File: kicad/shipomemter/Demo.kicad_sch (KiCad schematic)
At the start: 7 parts, among them J701 Conn_01x06_Pin, J702 Conn_01x06_Pin, J703 Conn_01x06_Pin, J704 Conn_01x06_Pin

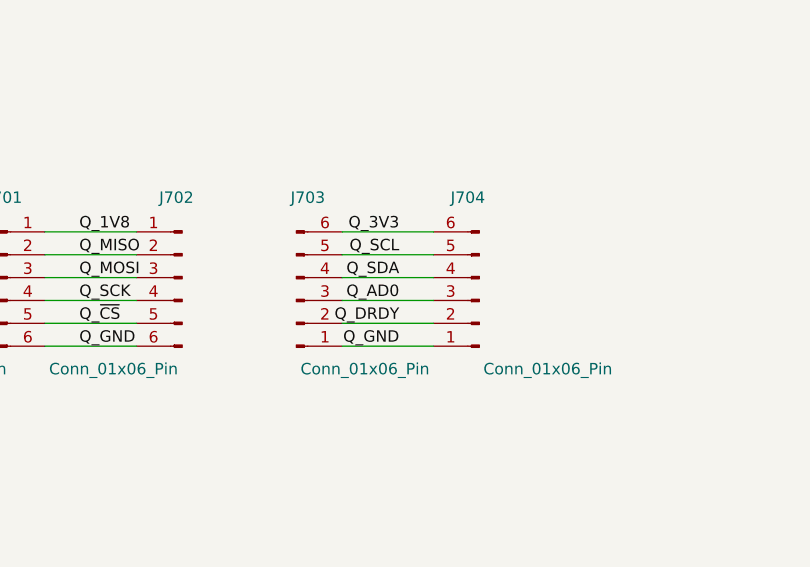
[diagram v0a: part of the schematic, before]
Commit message: Updated numbers on hand and numbers in cart
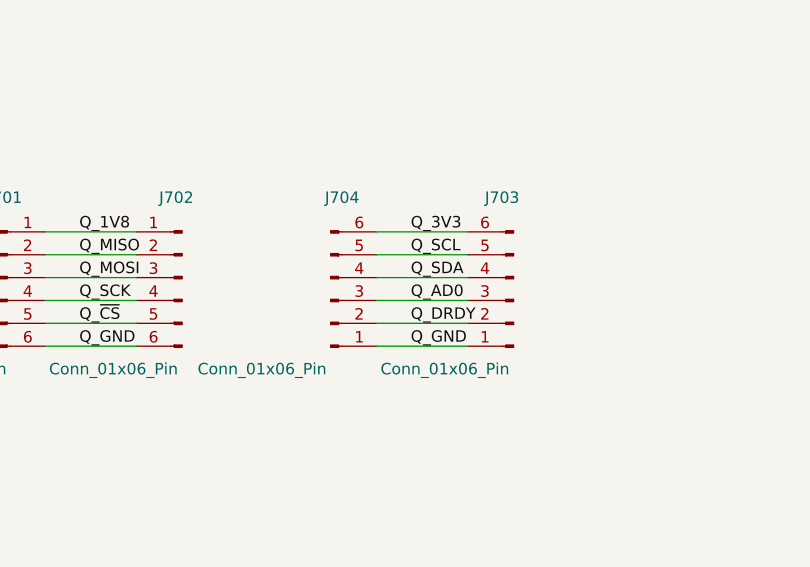
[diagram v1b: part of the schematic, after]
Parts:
- J701, J703: footprint Connector_PinHeader_2.54mm:PinHeader_1x06_P2.54mm_Vertical -> Connector_PinSocket_2.54mm:PinSocket_1x06_P2.54mm_Vertical; Mouser (none) -> 538-90147-1106; Number in cart (none) -> 2; Number on hand (none) -> 0
- J702, J704: Mouser (none) -> 855-M20-9990646; Number in cart (none) -> 2; Number on hand (none) -> 0
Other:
- moved on the sheet: J703, J704
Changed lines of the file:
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@@
   (junction (at 125.73 33.02) (diameter 0) (color 0 0 0 0)
   )
-  (wire (pts (xy 114.3 77.47) (xy 104.14 77.47))
+  (wire (pts (xy 107.95 77.47) (xy 118.11 77.47))
     (stroke (width 0) (type default))
   )
@@
     (stroke (width 0) (type default))
   )
-  (wire (pts (xy 114.3 80.01) (xy 104.14 80.01))
+  (wire (pts (xy 107.95 80.01) (xy 118.11 80.01))
     (stroke (width 0) (type default))
   )
@@
     (stroke (width 0) (type default))
   )
-  (wire (pts (xy 114.3 69.85) (xy 104.14 69.85))
-    (stroke (width 0) (type default))
-  )
-  (wire (pts (xy 114.3 74.93) (xy 104.14 74.93))
-    (stroke (width 0) (type default))
-  )
-  (wire (pts (xy 114.3 82.55) (xy 104.14 82.55))
+  (wire (pts (xy 107.95 69.85) (xy 118.11 69.85))
+    (stroke (width 0) (type default))
+  )
+  (wire (pts (xy 107.95 74.93) (xy 118.11 74.93))
+    (stroke (width 0) (type default))
+  )
+  (wire (pts (xy 107.95 82.55) (xy 118.11 82.55))
     (stroke (width 0) (type default))
   )
@@
     (stroke (width 0) (type default))
   )
-  (wire (pts (xy 114.3 72.39) (xy 104.14 72.39))
+  (wire (pts (xy 107.95 72.39) (xy 118.11 72.39))
     (stroke (width 0) (type default))
   )
@@
     (effects (font (size 1.27 1.27)) (justify left bottom))
   )
-  (label "Q_SCL" (at 110.49 72.39 180) (fields_autoplaced)
-    (effects (font (size 1.27 1.27)) (justify right bottom))
+  (label "Q_SCL" (at 111.76 72.39 0) (fields_autoplaced)
+    (effects (font (size 1.27 1.27)) (justify left bottom))
   )
   (label "Q_1V8" (at 74.93 69.85 0) (fields_autoplaced)
     (effects (font (size 1.27 1.27)) (justify left bottom))
   )
-  (label "Q_DRDY" (at 110.49 80.01 180) (fields_autoplaced)
-    (effects (font (size 1.27 1.27)) (justify right bottom))
-  )
-  (label "Q_3V3" (at 110.49 69.85 180) (fields_autoplaced)
-    (effects (font (size 1.27 1.27)) (justify right bottom))
+  (label "Q_DRDY" (at 111.76 80.01 0) (fields_autoplaced)
+    (effects (font (size 1.27 1.27)) (justify left bottom))
+  )
+  (label "Q_3V3" (at 111.76 69.85 0) (fields_autoplaced)
+    (effects (font (size 1.27 1.27)) (justify left bottom))
   )
   (label "Q_GND" (at 135.89 38.1 180) (fields_autoplaced)
@@
     (effects (font (size 1.27 1.27)) (justify left bottom))
   )
-  (label "Q_GND" (at 110.49 82.55 180) (fields_autoplaced)
-    (effects (font (size 1.27 1.27)) (justify right bottom))
-  )
-  (label "Q_SDA" (at 110.49 74.93 180) (fields_autoplaced)
-    (effects (font (size 1.27 1.27)) (justify right bottom))
+  (label "Q_GND" (at 111.76 82.55 0) (fields_autoplaced)
+    (effects (font (size 1.27 1.27)) (justify left bottom))
+  )
+  (label "Q_SDA" (at 111.76 74.93 0) (fields_autoplaced)
+    (effects (font (size 1.27 1.27)) (justify left bottom))
   )
   (label "Q_MISO" (at 74.93 72.39 0) (fields_autoplaced)
@@
     (effects (font (size 1.27 1.27)) (justify right bottom))
   )
-  (label "Q_AD0" (at 110.49 77.47 180) (fields_autoplaced)
-    (effects (font (size 1.27 1.27)) (justify right bottom))
+  (label "Q_AD0" (at 111.76 77.47 0) (fields_autoplaced)
+    (effects (font (size 1.27 1.27)) (justify left bottom))
   )
   (symbol (lib_id "KwanSystems:DesignedWithKicad") (at 212.09 173.99 0) (unit 1)
@@
     )
   )
-  (symbol (lib_id "Connector:Conn_01x06_Pin") (at 119.38 77.47 180) (unit 1)
-    (in_bom yes) (on_board yes) (dnp no)
-    (property "Reference" "J704" (at 118.11 66.04 0)
-      (effects (font (size 1.27 1.27)))
-    )
-    (property "Value" "Conn_01x06_Pin" (at 127 85.09 0)
-      (effects (font (size 1.27 1.27)))
-    )
-    (property "Footprint" "Connector_PinHeader_2.54mm:PinHeader_1x06_P2.54mm_Vertical" (at 119.38 77.47 0)
-      (effects (font (size 1.27 1.27)) hide)
-    )
-    (property "Datasheet" "~" (at 119.38 77.47 0)
+  (symbol (lib_id "Connector:Conn_01x06_Pin") (at 102.87 77.47 0) (mirror x) (unit 1)
+    (in_bom yes) (on_board yes) (dnp no)
+    (property "Reference" "J704" (at 104.14 66.04 0)
+      (effects (font (size 1.27 1.27)))
+    )
+    (property "Value" "Conn_01x06_Pin" (at 95.25 85.09 0)
+      (effects (font (size 1.27 1.27)))
+    )
+    (property "Footprint" "Connector_PinHeader_2.54mm:PinHeader_1x06_P2.54mm_Vertical" (at 102.87 77.47 0)
+      (effects (font (size 1.27 1.27)) hide)
+    )
+    (property "Datasheet" "~" (at 102.87 77.47 0)
+      (effects (font (size 1.27 1.27)) hide)
+    )
+    (property "Mouser" "855-M20-9990646" (at 102.87 77.47 0)
+      (effects (font (size 1.27 1.27)) hide)
+    )
+    (property "Number in cart" "2" (at 102.87 77.47 0)
+      (effects (font (size 1.27 1.27)) hide)
+    )
+    (property "Number on hand" "0" (at 102.87 77.47 0)
       (effects (font (size 1.27 1.27)) hide)
     )
@@
     )
   )
-  (symbol (lib_id "Connector:Conn_01x06_Pin") (at 99.06 77.47 0) (mirror x) (unit 1)
-    (in_bom yes) (on_board yes) (dnp no)
-    (property "Reference" "J703" (at 100.33 66.04 0)
-      (effects (font (size 1.27 1.27)))
-    )
-    (property "Value" "Conn_01x06_Pin" (at 106.68 85.09 0)
-      (effects (font (size 1.27 1.27)))
-    )
-    (property "Footprint" "Connector_PinHeader_2.54mm:PinHeader_1x06_P2.54mm_Vertical" (at 99.06 77.47 0)
-      (effects (font (size 1.27 1.27)) hide)
-    )
-    (property "Datasheet" "~" (at 99.06 77.47 0)
+  (symbol (lib_id "Connector:Conn_01x06_Pin") (at 123.19 77.47 180) (unit 1)
+    (in_bom yes) (on_board yes) (dnp no)
+    (property "Reference" "J703" (at 121.92 66.04 0)
+      (effects (font (size 1.27 1.27)))
+    )
+    (property "Value" "Conn_01x06_Pin" (at 115.57 85.09 0)
+      (effects (font (size 1.27 1.27)))
+    )
+    (property "Footprint" "Connector_PinSocket_2.54mm:PinSocket_1x06_P2.54mm_Vertical" (at 123.19 77.47 0)
+      (effects (font (size 1.27 1.27)) hide)
+    )
+    (property "Datasheet" "~" (at 123.19 77.47 0)
+      (effects (font (size 1.27 1.27)) hide)
+    )
+    (property "Mouser" "538-90147-1106" (at 123.19 77.47 0)
+      (effects (font (size 1.27 1.27)) hide)
+    )
+    (property "Number in cart" "2" (at 123.19 77.47 0)
+      (effects (font (size 1.27 1.27)) hide)
+    )
+    (property "Number on hand" "0" (at 123.19 77.47 0)
       (effects (font (size 1.27 1.27)) hide)
     )
@@
       (effects (font (size 1.27 1.27)) hide)
     )
+    (property "Mouser" "855-M20-9990646" (at 86.36 74.93 0)
+      (effects (font (size 1.27 1.27)) hide)
+    )
+    (property "Number in cart" "2" (at 86.36 74.93 0)
+      (effects (font (size 1.27 1.27)) hide)
+    )
+    (property "Number on hand" "0" (at 86.36 74.93 0)
+      (effects (font (size 1.27 1.27)) hide)
+    )
     (pin "1")
     (pin "2")
@@
       (effects (font (size 1.27 1.27)))
     )
-    (property "Footprint" "Connector_PinHeader_2.54mm:PinHeader_1x06_P2.54mm_Vertical" (at 66.04 74.93 0)
+    (property "Footprint" "Connector_PinSocket_2.54mm:PinSocket_1x06_P2.54mm_Vertical" (at 66.04 74.93 0)
       (effects (font (size 1.27 1.27)) hide)
     )
@@
       (effects (font (size 1.27 1.27)) hide)
     )
+    (property "Mouser" "538-90147-1106" (at 66.04 74.93 0)
+      (effects (font (size 1.27 1.27)) hide)
+    )
+    (property "Number in cart" "2" (at 66.04 74.93 0)
+      (effects (font (size 1.27 1.27)) hide)
+    )
+    (property "Number on hand" "0" (at 66.04 74.93 0)
+      (effects (font (size 1.27 1.27)) hide)
+    )

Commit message: Updated number on hand, and added more Digikey/Mouser/Mfg numbers
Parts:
- J701, J703: Digikey (none) -> WM4223-ND; Number in cart 2 -> (none); Number on hand 0 -> 2; Part Number (none) -> 90147-1106
- J702, J704: Digikey (none) -> 952-2270-ND; Number in cart 2 -> (none); Number on hand 0 -> 2; Part Number (none) -> M20-9990646
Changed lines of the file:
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@@
       (effects (font (size 1.27 1.27)) hide)
     )
-    (property "Number in cart" "2" (at 102.87 77.47 0)
+    (property "Number in cart" "" (at 102.87 77.47 0)
       (effects (font (size 1.27 1.27)) hide)
     )
-    (property "Number on hand" "0" (at 102.87 77.47 0)
+    (property "Number on hand" "2" (at 102.87 77.47 0)
+      (effects (font (size 1.27 1.27)) hide)
+    )
+    (property "Digikey" "952-2270-ND" (at 102.87 77.47 0)
+      (effects (font (size 1.27 1.27)) hide)
+    )
+    (property "Part Number" "M20-9990646" (at 102.87 77.47 0)
       (effects (font (size 1.27 1.27)) hide)
     )
@@
       (effects (font (size 1.27 1.27)) hide)
     )
-    (property "Number in cart" "2" (at 123.19 77.47 0)
+    (property "Number in cart" "" (at 123.19 77.47 0)
       (effects (font (size 1.27 1.27)) hide)
     )
-    (property "Number on hand" "0" (at 123.19 77.47 0)
+    (property "Number on hand" "2" (at 123.19 77.47 0)
+      (effects (font (size 1.27 1.27)) hide)
+    )
+    (property "Part Number" "90147-1106" (at 123.19 77.47 0)
+      (effects (font (size 1.27 1.27)) hide)
+    )
+    (property "Digikey" "WM4223-ND" (at 123.19 77.47 0)
       (effects (font (size 1.27 1.27)) hide)
     )
@@
       (effects (font (size 1.27 1.27)) hide)
     )
-    (property "Number in cart" "2" (at 86.36 74.93 0)
+    (property "Number in cart" "" (at 86.36 74.93 0)
       (effects (font (size 1.27 1.27)) hide)
     )
-    (property "Number on hand" "0" (at 86.36 74.93 0)
+    (property "Number on hand" "2" (at 86.36 74.93 0)
+      (effects (font (size 1.27 1.27)) hide)
+    )
+    (property "Digikey" "952-2270-ND" (at 86.36 74.93 0)
+      (effects (font (size 1.27 1.27)) hide)
+    )
+    (property "Part Number" "M20-9990646" (at 86.36 74.93 0)
       (effects (font (size 1.27 1.27)) hide)
     )
@@
       (effects (font (size 1.27 1.27)) hide)
     )
-    (property "Number in cart" "2" (at 66.04 74.93 0)
+    (property "Number in cart" "" (at 66.04 74.93 0)
       (effects (font (size 1.27 1.27)) hide)
     )
-    (property "Number on hand" "0" (at 66.04 74.93 0)
+    (property "Number on hand" "2" (at 66.04 74.93 0)
       (effects (font (size 1.27 1.27)) hide)
     )
+    (property "Part Number" "90147-1106" (at 66.04 74.93 0)
+      (effects (font (size 1.27 1.27)) hide)
+    )
+    (property "Digikey" "WM4223-ND" (at 66.04 74.93 0)
+      (effects (font (size 1.27 1.27)) hide)
+    )
